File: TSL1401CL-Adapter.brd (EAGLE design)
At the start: 31.8 x 31.8 mm, 4 parts

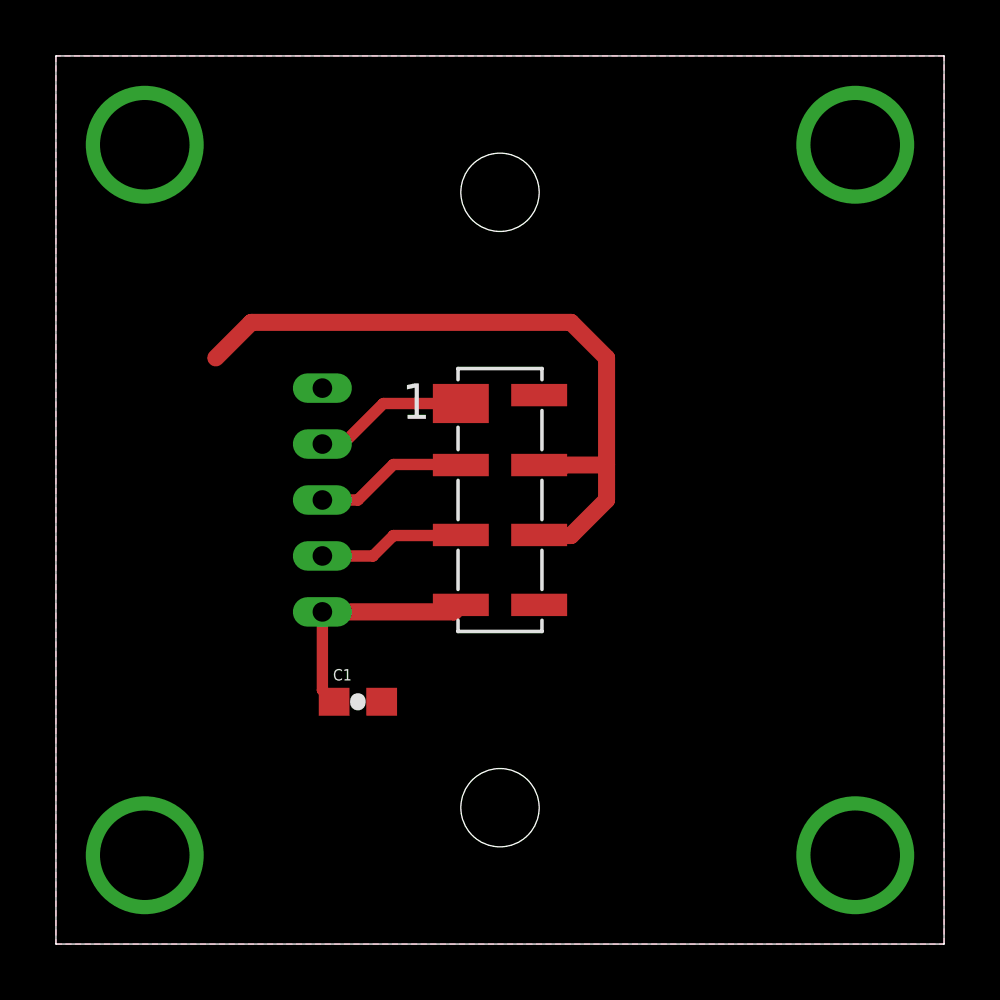
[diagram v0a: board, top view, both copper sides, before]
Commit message: Put the capacitor on the bottom, and adjusted position of connector to fit PT-LH011M from m12lenses.com
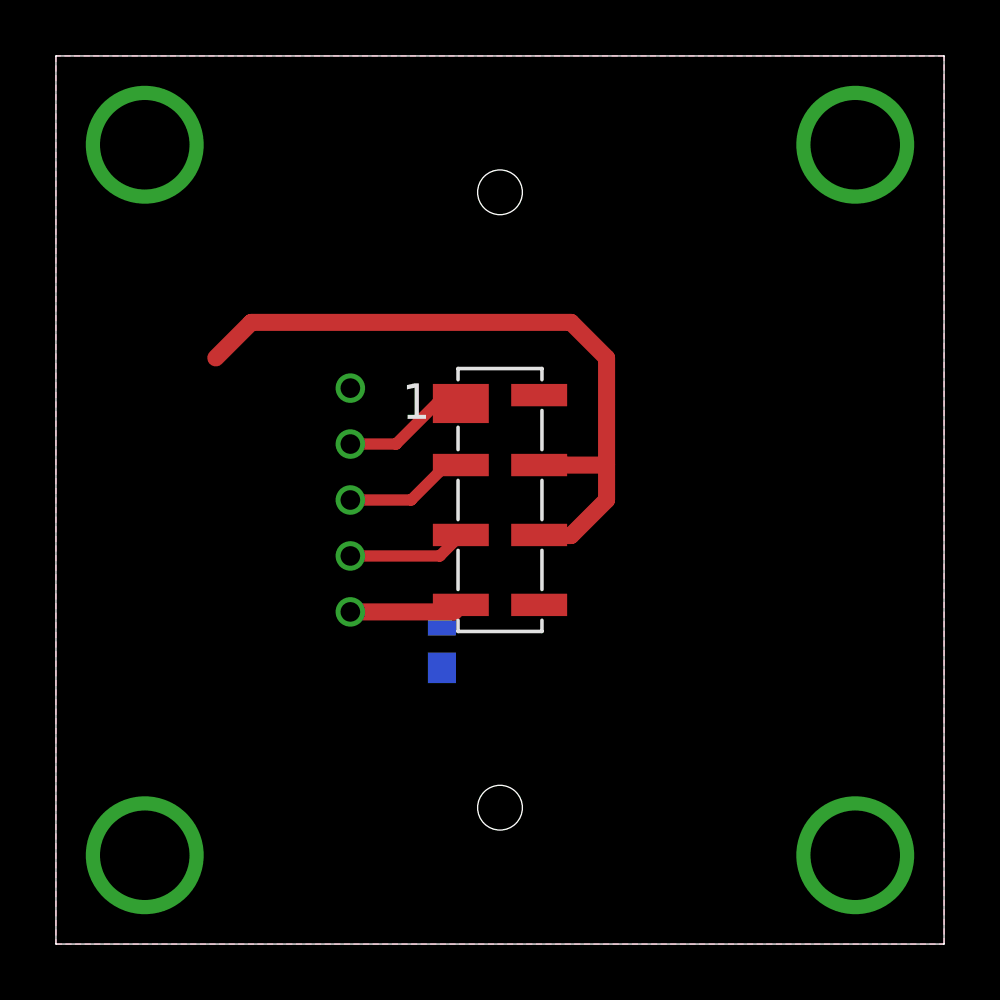
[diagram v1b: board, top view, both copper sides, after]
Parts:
- moved C1 3.64 mm to (13.2, 10.1), flipped to the bottom, turned to 270 degrees
- moved U$3 1.00 mm to (9.89, 15.2)
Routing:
- net +5V: track 8.44 -> 7.42 mm
- net CLK: track 5.48 -> 4.48 mm
- net SI: track 5.55 -> 4.55 mm
- net AO: track 5.26 -> 4.26 mm
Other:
- board text added: "September 30, 2013"
- board text removed: "April 30, 2013"
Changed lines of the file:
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@@
 <setting verticaltext="up"/>
 </settings>
-<grid distance="50" unitdist="mil" unit="mil" style="lines" multiple="1" display="yes" altdistance="5" altunitdist="mil" altunit="mil"/>
+<grid distance="25" unitdist="mil" unit="mil" style="lines" multiple="1" display="yes" altdistance="5" altunitdist="mil" altunit="mil"/>
 <layers>
 <layer number="1" name="Top" color="4" fill="1" visible="yes" active="yes"/>
@@
 <layer number="22" name="bPlace" color="14" fill="1" visible="yes" active="yes"/>
 <layer number="23" name="tOrigins" color="15" fill="1" visible="yes" active="yes"/>
-<layer number="24" name="bOrigins" color="15" fill="1" visible="no" active="yes"/>
-<layer number="25" name="tNames" color="7" fill="1" visible="yes" active="yes"/>
+<layer number="24" name="bOrigins" color="15" fill="1" visible="yes" active="yes"/>
+<layer number="25" name="tNames" color="7" fill="1" visible="no" active="yes"/>
 <layer number="26" name="bNames" color="7" fill="1" visible="no" active="yes"/>
 <layer number="27" name="tValues" color="7" fill="1" visible="no" active="yes"/>
@@
 <layer number="42" name="bRestrict" color="1" fill="10" visible="no" active="yes"/>
 <layer number="43" name="vRestrict" color="2" fill="10" visible="no" active="yes"/>
-<layer number="44" name="Drills" color="7" fill="1" visible="yes" active="yes"/>
+<layer number="44" name="Drills" color="7" fill="1" visible="no" active="yes"/>
 <layer number="45" name="Holes" color="7" fill="1" visible="yes" active="yes"/>
 <layer number="46" name="Milling" color="3" fill="1" visible="no" active="yes"/>
@@
 <text x="20.32" y="3.81" size="1.016" layer="22" font="vector" ratio="15" rot="MR90">University of Massachusetts</text>
 <text x="19.05" y="3.81" size="1.016" layer="22" font="vector" ratio="15" rot="MR90">Medical School</text>
-<text x="17.78" y="3.81" size="1.016" layer="22" font="vector" ratio="15" rot="MR90">April 30, 2013</text>
+<text x="17.78" y="3.81" size="1.016" layer="22" font="vector" ratio="15" rot="MR90">September 30, 2013</text>
 <dimension x1="27.94" y1="27.94" x2="27.94" y2="2.54" x3="34.29" y3="15.24" textsize="1.778" layer="51" dtype="vertical"/>
 <dimension x1="15.24" y1="15.24" x2="-0.635" y2="15.24" x3="7.3025" y3="33.02" textsize="1.778" layer="51" dtype="vertical"/>
@@
 <dimension x1="15.24" y1="15.24" x2="2.54" y2="27.94" x3="-2.54" y3="21.59" textsize="1.778" layer="51" dtype="vertical"/>
 <dimension x1="15.24" y1="15.24" x2="27.94" y2="15.24" x3="21.59" y3="-3.81" textsize="1.778" layer="51" dtype="horizontal"/>
-<dimension x1="-0.635" y1="0.127" x2="31.115" y2="0" x3="15.24" y3="-8.89" textsize="1.778" layer="51" dtype="horizontal"/>
+<dimension x1="-0.635" y1="0.127" x2="31.115" y2="0" x3="15.24" y3="-10.89" textsize="1.778" layer="51" dtype="horizontal"/>
+<dimension x1="6.75" y1="7.492" x2="23.623" y2="7.492" x3="15.1865" y3="-7" textsize="1.778" layer="51" dtype="horizontal"/>
+<dimension x1="9.017" y1="6.4424" x2="9.159" y2="24.004" x3="3" y3="15.2232" textsize="1.778" layer="51" dtype="vertical"/>
+<dimension x1="15.25" y1="26.25" x2="15.25" y2="4.25" x3="-10" y3="15.25" textsize="1.778" layer="51" dtype="vertical"/>
 </plain>
 <attributes>
@@
 <element name="U$1" library="BIG" package="TSL1401CL" value="TSL1401CL" x="15.24" y="15.24"/>
 <element name="U$2" library="SparkFun" package="OSHW-LOGO-M" value="OSHW-LOGOM" x="8.89" y="25.4" rot="MR0"/>
-<element name="C1" library="SparkFun-Passives" package="0603-CAP" value="1uF (16V)" x="10.16" y="8.0264"/>
-<element name="U$3" library="BIG" package="M05JST-PTH" value="M05" x="8.89" y="15.24" rot="MR180"/>
+<element name="C1" library="SparkFun-Passives" package="0603-CAP" value="1uF (16V)" x="13.1614" y="10.09" smashed="yes" rot="MR270">
+<attribute name="NAME" x="12.3994" y="10.979" size="0.4064" layer="26" font="vector" rot="MR270"/>
+<attribute name="VALUE" x="14.3044" y="11.106" size="0.4064" layer="28" font="vector" rot="MR270"/>
+</element>
+<element name="U$3" library="BIG" package="M05JST-PTH" value="M05" x="9.89" y="15.24" rot="MR180"/>
 </elements>
 <signals>
@@
 <contactref element="C1" pad="1"/>
 <contactref element="U$3" pad="P$5"/>
-<wire x1="8.89" y1="11.24" x2="13.59" y2="11.24" width="0.6096" layer="1"/>
+<wire x1="9.89" y1="11.24" x2="13.59" y2="11.24" width="0.6096" layer="1"/>
 <wire x1="13.59" y1="11.24" x2="13.84" y2="11.49" width="0.6096" layer="1"/>
-<wire x1="8.89" y1="11.24" x2="8.89" y2="8.4464" width="0.4064" layer="1"/>
-<wire x1="8.89" y1="8.4464" x2="9.31" y2="8.0264" width="0.4064" layer="1"/>
+<wire x1="9.89" y1="11.24" x2="12.7264" y2="11.24" width="0.4064" layer="16"/>
+<wire x1="12.7264" y1="11.24" x2="13.1614" y2="10.94" width="0.4064" layer="16"/>
 </signal>
 <signal name="GND">
@@
 <contactref element="U$1" pad="SI"/>
 <contactref element="U$3" pad="P$2"/>
-<wire x1="9.62" y1="17.24" x2="8.89" y2="17.24" width="0.4064" layer="1"/>
-<wire x1="9.62" y1="17.24" x2="11.07" y2="18.69" width="0.4064" layer="1"/>
-<wire x1="11.07" y1="18.69" x2="13.84" y2="18.69" width="0.4064" layer="1"/>
+<wire x1="9.89" y1="17.24" x2="11.525" y2="17.24" width="0.4064" layer="1"/>
+<wire x1="11.525" y1="17.24" x2="12.975" y2="18.69" width="0.4064" layer="1"/>
+<wire x1="13.84" y1="18.69" x2="12.975" y2="18.69" width="0.4064" layer="1"/>
 </signal>
 <signal name="AO">
 <contactref element="U$1" pad="AO"/>
-<wire x1="11.43" y1="13.97" x2="13.82" y2="13.97" width="0.4064" layer="1"/>
-<wire x1="13.82" y1="13.97" x2="13.84" y2="13.99" width="0.4064" layer="1"/>
 <contactref element="U$3" pad="P$4"/>
-<wire x1="10.7" y1="13.24" x2="11.43" y2="13.97" width="0.4064" layer="1"/>
-<wire x1="10.7" y1="13.24" x2="8.89" y2="13.24" width="0.4064" layer="1"/>
+<wire x1="9.89" y1="13.24" x2="13.09" y2="13.24" width="0.4064" layer="1"/>
+<wire x1="13.09" y1="13.24" x2="13.84" y2="13.99" width="0.4064" layer="1"/>
 </signal>
 <signal name="CLK">
 <contactref element="U$1" pad="CLK"/>
 <contactref element="U$3" pad="P$3"/>
-<wire x1="8.89" y1="15.24" x2="10.16" y2="15.24" width="0.4064" layer="1"/>
-<wire x1="10.16" y1="15.24" x2="11.43" y2="16.51" width="0.4064" layer="1"/>
-<wire x1="11.43" y1="16.51" x2="13.82" y2="16.51" width="0.4064" layer="1"/>
+<wire x1="9.89" y1="15.24" x2="12.065" y2="15.24" width="0.4064" layer="1"/>
+<wire x1="12.065" y1="15.24" x2="13.335" y2="16.51" width="0.4064" layer="1"/>
+<wire x1="13.335" y1="16.51" x2="13.82" y2="16.51" width="0.4064" layer="1"/>
 <wire x1="13.82" y1="16.51" x2="13.84" y2="16.49" width="0.4064" layer="1"/>
 </signal>
